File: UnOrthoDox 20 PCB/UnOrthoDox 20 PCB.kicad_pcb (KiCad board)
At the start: 2 copper layers, 76.2 x 94.2 mm, 81 parts, among them J1 Conn_01x02, SW1 SW_MX_HotSwap, SW10 SW_MX_HotSwap, SW11 SW_MX_HotSwap, SW12 SW_MX_HotSwap, SW13 SW_MX_HotSwap, SW14 SW_MX_HotSwap, SW15 SW_MX_HotSwap, SW16 SW_MX_HotSwap, SW16A1 SW_MX_HotSwap, SW17 SW_MX_HotSwap, SW17A1 SW_MX_HotSwap, SW18 SW_MX_HotSwap, SW19 SW_MX_HotSwap, SW2 SW_MX_HotSwap, SW20 SW_MX_HotSwap, SW3 SW_MX_HotSwap, SW4 SW_MX_HotSwap, SW5 SW_MX_HotSwap, SW6 SW_MX_HotSwap, SW7 SW_MX_HotSwap, SW8 SW_MX_HotSwap, SW8A1 SW_MX_HotSwap, SW9 SW_MX_HotSwap, U1 ProMicro

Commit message: Added 17
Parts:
- removed J1: Conn_01x02, Connector_PinHeader_2.54mm:PinHeader_1x02_P2.54mm_Vertical
- removed LED16A1, LED17A1, LED8A1: SK6812, Keyboard RGB:RGB_SK6812MINI-E
- removed RES1: TS-A002, Keyboard Common:YTS-A002
- removed ST1, ST2, ST3: Stabilizer_2u_MX, Keyboard Stabilizer:Stabilizer_Cherry_MX_2.00u
- removed SW16A1, SW17A1, SW8A1: SW_MX_HotSwap, Keyboard Switches:SW_MX_HotSwap
- removed SW_SLIDE_1: MSK12C02, Keyboard Common:MSK12C02
- added RZ1: RP2040-Zero, Keyboard Controllers:RP2040-Zero_reverse_mount_flipped, B.Cu at (147.8, 54.7)
- C1, C2, C3, C4: value 100nF -> C_Small; footprint Capacitor_SMD:C_0805_2012Metric_Pad1.18x1.45mm_HandSolder -> Capacitor_SMD:C_0603_1608Metric_Pad1.08x0.95mm_HandSolder
- ENC1, ENC2: footprint Keyboard Encoders:Encoder_Alps_EC11E_Offset_pad -> Keyboard Encoders:Encoder_Alps_EC11E_Small
- RGB1: renamed from LED1; value SK6812 -> SK6812MINI-E; footprint Keyboard RGB:RGB_SK6812MINI-E -> Keyboard RGB:MX_SK6812MINI-E_REVERSIBLE
- RGB10: renamed from LED10; value SK6812 -> SK6812MINI-E; footprint Keyboard RGB:RGB_SK6812MINI-E -> Keyboard RGB:MX_SK6812MINI-E_REVERSIBLE
- RGB11: renamed from LED11; value SK6812 -> SK6812MINI-E; footprint Keyboard RGB:RGB_SK6812MINI-E -> Keyboard RGB:MX_SK6812MINI-E_REVERSIBLE
- RGB12: renamed from LED12; value SK6812 -> SK6812MINI-E; footprint Keyboard RGB:RGB_SK6812MINI-E -> Keyboard RGB:MX_SK6812MINI-E_REVERSIBLE
- RGB13: renamed from LED13; value SK6812 -> SK6812MINI-E; footprint Keyboard RGB:RGB_SK6812MINI-E -> Keyboard RGB:MX_SK6812MINI-E_REVERSIBLE
- RGB14: renamed from LED14; value SK6812 -> SK6812MINI-E; footprint Keyboard RGB:RGB_SK6812MINI-E -> Keyboard RGB:MX_SK6812MINI-E_REVERSIBLE
- RGB15: renamed from LED15; value SK6812 -> SK6812MINI-E; footprint Keyboard RGB:RGB_SK6812MINI-E -> Keyboard RGB:MX_SK6812MINI-E_REVERSIBLE
- RGB16: renamed from LED16; value SK6812 -> SK6812MINI-E; footprint Keyboard RGB:RGB_SK6812MINI-E -> Keyboard RGB:MX_SK6812MINI-E_REVERSIBLE
- RGB17: renamed from LED17; value SK6812 -> SK6812MINI-E; footprint Keyboard RGB:RGB_SK6812MINI-E -> Keyboard RGB:MX_SK6812MINI-E_REVERSIBLE
- RGB18: renamed from LED18; value SK6812 -> SK6812MINI-E; footprint Keyboard RGB:RGB_SK6812MINI-E -> Keyboard RGB:MX_SK6812MINI-E_REVERSIBLE
- RGB19: renamed from LED19; value SK6812 -> SK6812MINI-E; footprint Keyboard RGB:RGB_SK6812MINI-E -> Keyboard RGB:MX_SK6812MINI-E_REVERSIBLE
- RGB2: renamed from LED2; value SK6812 -> SK6812MINI-E; footprint Keyboard RGB:RGB_SK6812MINI-E -> Keyboard RGB:MX_SK6812MINI-E_REVERSIBLE
- RGB20: renamed from LED20; value SK6812 -> SK6812MINI-E; footprint Keyboard RGB:RGB_SK6812MINI-E -> Keyboard RGB:MX_SK6812MINI-E_REVERSIBLE
- RGB3: renamed from LED3; value SK6812 -> SK6812MINI-E; footprint Keyboard RGB:RGB_SK6812MINI-E -> Keyboard RGB:MX_SK6812MINI-E_REVERSIBLE
- RGB4: renamed from LED4; value SK6812 -> SK6812MINI-E; footprint Keyboard RGB:RGB_SK6812MINI-E -> Keyboard RGB:MX_SK6812MINI-E_REVERSIBLE
- RGB5: renamed from LED5; value SK6812 -> SK6812MINI-E; footprint Keyboard RGB:RGB_SK6812MINI-E -> Keyboard RGB:MX_SK6812MINI-E_REVERSIBLE
- RGB6: renamed from LED6; value SK6812 -> SK6812MINI-E; footprint Keyboard RGB:RGB_SK6812MINI-E -> Keyboard RGB:MX_SK6812MINI-E_REVERSIBLE
- RGB7: renamed from LED7; value SK6812 -> SK6812MINI-E; footprint Keyboard RGB:RGB_SK6812MINI-E -> Keyboard RGB:MX_SK6812MINI-E_REVERSIBLE
- RGB8: renamed from LED8; value SK6812 -> SK6812MINI-E; footprint Keyboard RGB:RGB_SK6812MINI-E -> Keyboard RGB:MX_SK6812MINI-E_REVERSIBLE
- RGB9: renamed from LED9; value SK6812 -> SK6812MINI-E; footprint Keyboard RGB:RGB_SK6812MINI-E -> Keyboard RGB:MX_SK6812MINI-E_REVERSIBLE
- SW1, SW10, SW11, SW12, SW13, SW14, SW15, SW16, SW17, SW18, SW19, SW2, SW20, SW3, SW4, SW5, SW6, SW7, SW8, SW9: footprint Keyboard Switches:SW_MX_HotSwap -> Keyboard Switches:SW_MX_HotSwap_Reversible
- U1: value ProMicro -> SN74LV1T34DBV; footprint Keyboard Controllers:ArduinoProMicro-BackSide_special -> Package_TO_SOT_SMD:SOT-23-5; moved to B.Cu
- moved D18 16.0 mm to (130.6, 121.4)
- moved RGB16 15.2 mm to (176.9, 104.9), turned to 180 degrees
- moved RGB8 15.2 mm to (176.9, 66.8), turned to 180 degrees
- moved U1 13.6 mm to (126.3, 52.2), turned to 180 degrees
- moved RGB18 6.08 mm to (138.8, 123.9), turned to 180 degrees
- moved D20 5.28 mm to (168.7, 121.4)
- moved D12 5.10 mm to (168.8, 83.6)
- moved RGB1 5.08 mm to (119.8, 47.7), turned to 180 degrees
- moved RGB2 5.08 mm to (138.8, 47.7), turned to 180 degrees
- moved RGB3 5.08 mm to (157.9, 47.7), turned to 180 degrees
- moved RGB4 5.08 mm to (176.9, 47.7), turned to 180 degrees
- moved RGB5 5.08 mm to (119.8, 66.8), turned to 180 degrees
- moved RGB6 5.08 mm to (138.8, 66.8), turned to 180 degrees
- moved RGB7 5.08 mm to (157.9, 66.8), turned to 180 degrees
- moved RGB10 5.08 mm to (138.8, 85.8), turned to 180 degrees
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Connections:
- net C renamed Net-(D17-A)
- net ENC1 renamed EncA
- net ENC2 renamed EncB
- C1 pad 1: Enc1A -> Enc_1
- C2 pad 2: Enc1B -> Enc_2
- C3 pad 1: Enc2A -> Enc_1
- C4 pad 2: Enc2B -> Enc_3
- D16 pad 2: B -> Net-(D16-A)
- D18 pad 2: Net-(D18-Pad2) -> Net-(D18-A)
- D8 pad 2: A -> Net-(D8-A)
- ENC1 pad A: Enc1A -> Enc_1
- ENC1 pad B: Enc1B -> Enc_2
- ENC2 pad A: Enc2A -> Enc_1
- ENC2 pad B: Enc2B -> Enc_3
- RGB1 pad 1: GND -> +5V
- RGB1 pad 2: RGB -> Net-(RGB1-DOUT)
- RGB1 pad 3: VCC -> GND
- RGB1 pad 4: Net-(LED1-Pad4) -> RGB_5
- RGB10 pad 1: GND -> +5V
- RGB10 pad 2: Net-(LED10-Pad2) -> Net-(RGB10-DOUT)
- RGB10 pad 3: VCC -> GND
- RGB10 pad 4: Net-(LED10-Pad4) -> Net-(RGB10-DIN)
- RGB11 pad 1: GND -> +5V
- RGB11 pad 2: Net-(LED10-Pad4) -> Net-(RGB11-DOUT)
- RGB11 pad 3: VCC -> GND
- RGB11 pad 4: Net-(LED11-Pad4) -> Net-(RGB10-DOUT)
- RGB12 pad 1: GND -> +5V
- RGB12 pad 2: Net-(LED11-Pad4) -> Net-(RGB12-DOUT)
- RGB12 pad 3: VCC -> GND
- RGB12 pad 4: Net-(LED12-Pad4) -> Net-(RGB11-DOUT)
- RGB13 pad 1: GND -> +5V
- RGB13 pad 3: VCC -> GND
- RGB13 pad 4: Net-(LED13-Pad4) -> Net-(RGB12-DOUT)
- RGB14 pad 1: GND -> +5V
- RGB14 pad 3: VCC -> GND
- RGB15 pad 1: GND -> +5V
- RGB15 pad 3: VCC -> GND
- RGB16 pad 1: GND -> +5V
- RGB16 pad 2: Net-(LED12-Pad4) -> Net-(RGB16-DOUT)
- RGB16 pad 3: VCC -> GND
- RGB17 pad 1: GND -> +5V
- RGB17 pad 2: Net-(LED13-Pad4) -> Net-(RGB17-DOUT)
- RGB17 pad 3: VCC -> GND
- RGB17 pad 4: Net-(LED17-Pad4) -> Net-(RGB16-DOUT)
- RGB18 pad 1: GND -> +5V
- RGB18 pad 2: Net-(LED17-Pad4) -> Net-(RGB18-DOUT)
- RGB18 pad 3: VCC -> GND
- RGB18 pad 4: Net-(LED17A1-Pad4) -> Net-(RGB17-DOUT)
- RGB19 pad 1: GND -> +5V
- RGB19 pad 2: Net-(LED17A1-Pad4) -> Net-(RGB19-DOUT)
- RGB19 pad 3: VCC -> GND
- RGB19 pad 4: Net-(LED19-Pad4) -> Net-(RGB18-DOUT)
- RGB2 pad 1: GND -> +5V
- RGB2 pad 2: Net-(LED1-Pad4) -> Net-(RGB2-DOUT)
- RGB2 pad 3: VCC -> GND
- RGB2 pad 4: Net-(LED2-Pad4) -> Net-(RGB1-DOUT)
- RGB20 pad 1: GND -> +5V
- RGB20 pad 2: Net-(LED19-Pad4) -> unconnected-(RGB20-DOUT-Pad2)
- RGB20 pad 3: VCC -> GND
- RGB20 pad 4: unconnected-(LED20-Pad4) -> Net-(RGB19-DOUT)
- RGB3 pad 1: GND -> +5V
- RGB3 pad 2: Net-(LED2-Pad4) -> Net-(RGB3-DOUT)
- RGB3 pad 3: VCC -> GND
- RGB3 pad 4: Net-(LED3-Pad4) -> Net-(RGB2-DOUT)
- RGB4 pad 1: GND -> +5V
- RGB4 pad 2: Net-(LED3-Pad4) -> Net-(RGB4-DOUT)
- RGB4 pad 3: VCC -> GND
- RGB4 pad 4: Net-(LED4-Pad4) -> Net-(RGB3-DOUT)
- RGB5 pad 1: GND -> +5V
- RGB5 pad 3: VCC -> GND
- RGB5 pad 4: Net-(LED5-Pad4) -> Net-(RGB4-DOUT)
- RGB6 pad 1: GND -> +5V
- RGB6 pad 3: VCC -> GND
- RGB7 pad 1: GND -> +5V
- RGB7 pad 3: VCC -> GND
- RGB8 pad 1: GND -> +5V
- RGB8 pad 2: Net-(LED4-Pad4) -> Net-(RGB8-DOUT)
- RGB8 pad 3: VCC -> GND
- RGB9 pad 1: GND -> +5V
- RGB9 pad 2: Net-(LED5-Pad4) -> Net-(RGB10-DIN)
- RGB9 pad 3: VCC -> GND
- RGB9 pad 4: Net-(LED10-Pad2) -> Net-(RGB8-DOUT)
- SW16 pad 1: Col3 -> Net-(D16-A)
- SW16 pad 2: B -> Col3
- SW18 pad 1: Col1 -> Net-(D18-A)
- SW18 pad 2: Net-(D18-Pad2) -> Col1
- SW8 pad 1: Col3 -> Net-(D8-A)
- SW8 pad 2: A -> Col3
- U1 pad 4: GND -> RGB_5
- U1 pad 5: Enc1B -> +5V
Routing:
- net +5V: track 0.00 -> 485.6 mm, vias 0 -> 25
- net VCC: track 410.0 -> 0.00 mm, vias 25 -> 0
- net Net-(RGB4-DOUT): track 0.00 -> 90.2 mm, vias 0 -> 4
- net Net-(RGB16-DOUT): track 0.00 -> 83.2 mm, vias 0 -> 3
- net Net-(RGB12-DOUT): track 0.00 -> 82.8 mm, vias 0 -> 3
- net Net-(RGB8-DOUT): track 0.00 -> 82.2 mm, vias 0 -> 3
- net Enc_1: track 0.00 -> 66.9 mm
- net /RAW: track 46.4 -> 0.00 mm, vias 1 -> 0
- net Net-(RGB15-DOUT): track 60.2 -> 17.9 mm, vias 4 -> 2
- net Net-(LED4-Pad4): track 41.9 -> 0.00 mm, vias 2 -> 0
- net Net-(RGB7-DOUT): track 58.4 -> 17.7 mm, vias 4 -> 2
- net Net-(LED13-Pad4): track 40.2 -> 0.00 mm, vias 2 -> 0
- net Net-(RES1-Pad1): track 40.0 -> 0.00 mm, vias 1 -> 0
- net Net-(LED12-Pad4): track 38.9 -> 0.00 mm, vias 2 -> 0
- net Net-(LED17A1-Pad4): track 38.6 -> 0.00 mm, vias 3 -> 0
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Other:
- board size 76.2 x 94.2 mm -> 76.2 x 96.7 mm
- board text removed: "- +"
- board text removed: "RESET"

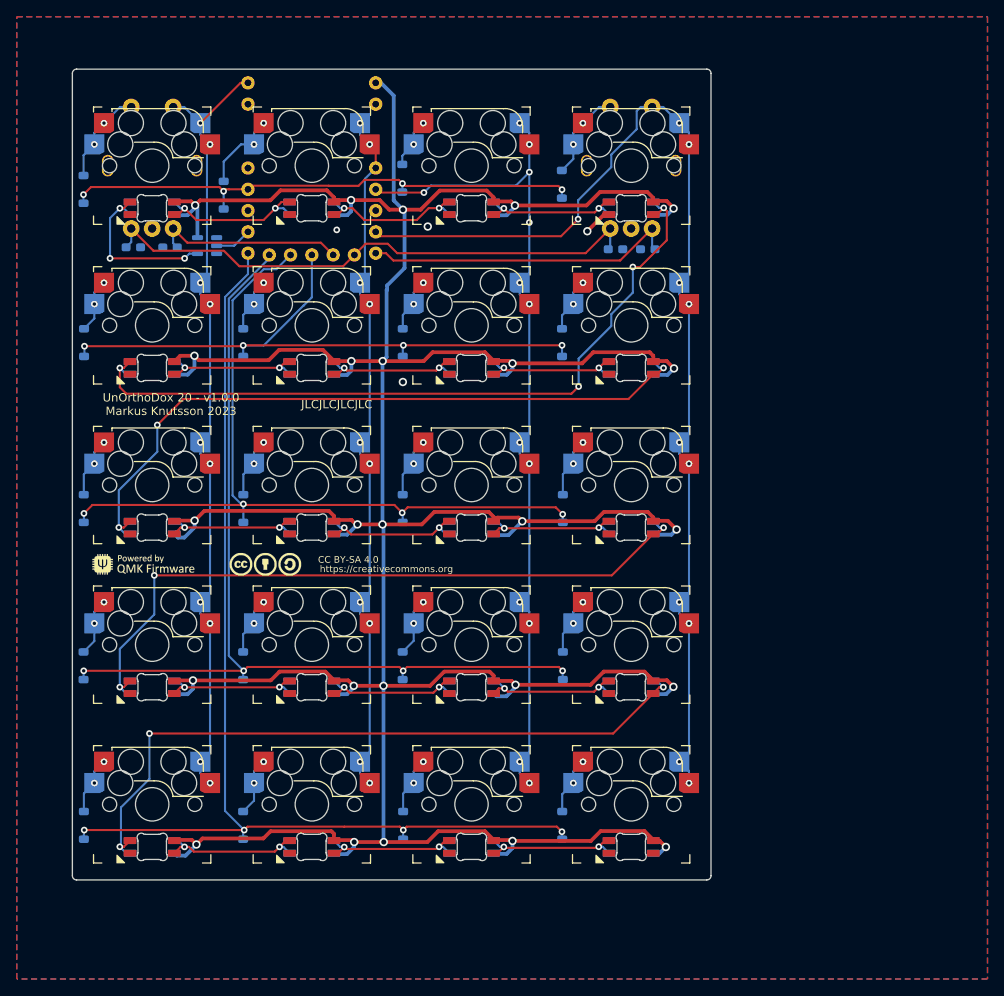
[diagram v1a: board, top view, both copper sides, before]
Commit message: Final tweaks 17/20 PCB
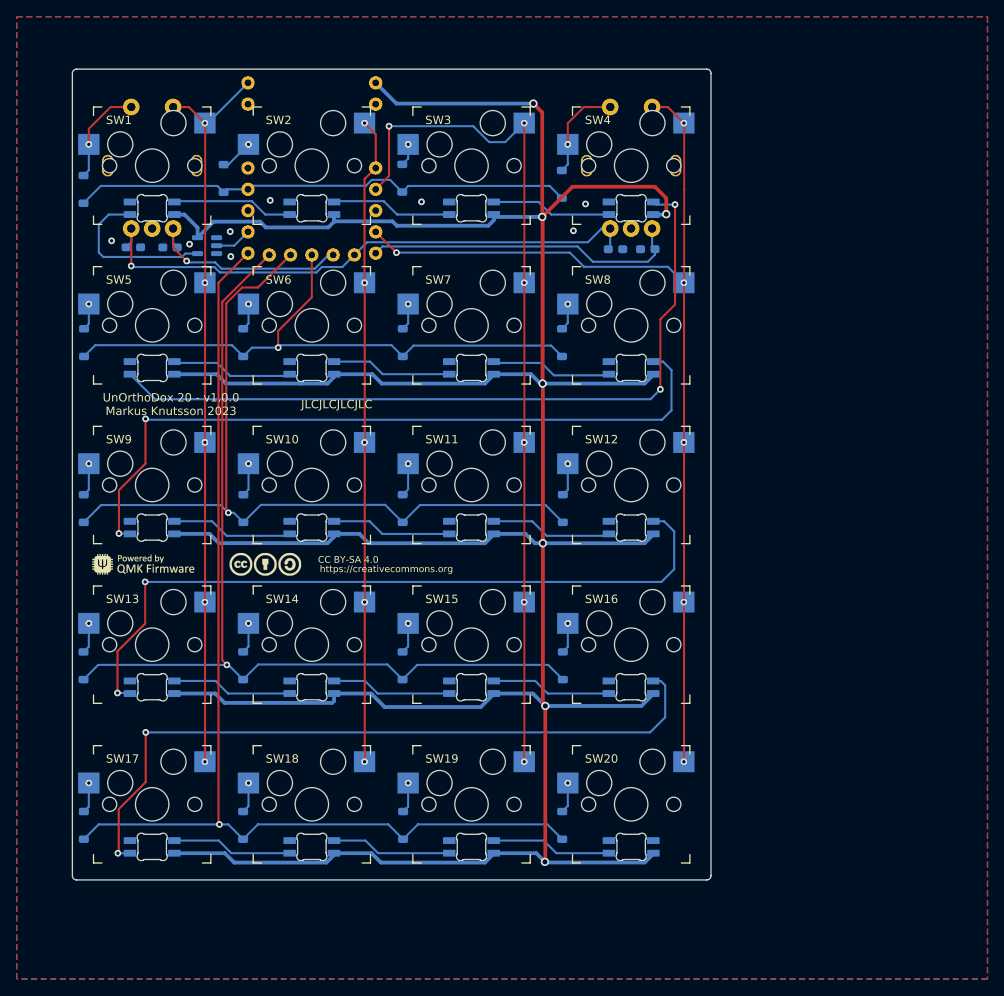
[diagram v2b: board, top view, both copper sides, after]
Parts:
- RGB1, RGB10, RGB11, RGB12, RGB13, RGB14, RGB15, RGB16, RGB17, RGB18, RGB19, RGB2, RGB20, RGB3, RGB4, RGB5, RGB6, RGB7, RGB8, RGB9: footprint Keyboard RGB:MX_SK6812MINI-E_REVERSIBLE -> Keyboard RGB:RGB_SK6812MINI-E
- RZ1: footprint Keyboard Controllers:RP2040-Zero_reverse_mount_flipped -> Keyboard Controllers:RP2040-Zero_reverse_mount_flipped_less_pins
- SW1, SW10, SW11, SW12, SW13, SW14, SW15, SW16, SW17, SW18, SW19, SW2, SW20, SW3, SW4, SW5, SW6, SW7, SW8, SW9: footprint Keyboard Switches:SW_MX_HotSwap_Reversible -> Keyboard Switches:SW_MX_HotSwap
- moved RGB17 5.08 mm to (119.8, 129.0)
- moved RGB18 5.08 mm to (138.8, 129.0)
- moved RGB19 5.08 mm to (157.9, 129.0)
- moved RGB20 5.08 mm to (176.9, 129.0)
- moved RGB1 5.08 mm to (119.8, 52.8)
- moved RGB10 5.08 mm to (138.8, 90.9)
- moved RGB11 5.08 mm to (157.9, 90.9)
- moved RGB12 5.08 mm to (176.9, 90.9)
- moved RGB13 5.08 mm to (119.8, 110.0)
- moved RGB14 5.08 mm to (138.8, 110.0)
- moved RGB15 5.08 mm to (157.9, 110.0)
- moved RGB16 5.08 mm to (176.9, 110.0)
- moved RGB2 5.08 mm to (138.8, 52.8)
- moved RGB3 5.08 mm to (157.9, 52.8)
- moved RGB4 5.08 mm to (176.9, 52.8)
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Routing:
- net +5V: track 485.6 -> 423.0 mm, vias 25 -> 7
- net Col3: track 130.1 -> 120.1 mm, vias 11 -> 6
- net Col0: track 94.7 -> 88.0 mm, vias 10 -> 5
- net Col1: track 83.6 -> 77.3 mm, vias 10 -> 5
- net Net-(D2-A): track 9.84 -> 3.96 mm, vias 2 -> 1
- net Row1: track 77.9 -> 73.1 mm, vias 4 -> 1
- net Net-(RGB8-DOUT): track 82.2 -> 87.0 mm, vias 3 -> 2
- net Net-(RGB1-DOUT): track 19.1 -> 14.5 mm, vias 2 -> 0
- net Net-(RGB12-DOUT): track 82.8 -> 87.4 mm, vias 3 -> 2
- net Net-(RGB2-DOUT): track 18.6 -> 14.5 mm, vias 2 -> 0
- net Net-(RGB10-DOUT): track 18.1 -> 14.4 mm, vias 2 -> 0
- net Net-(RGB14-DOUT): track 18.0 -> 14.4 mm, vias 2 -> 0
- net Row0: track 63.9 -> 60.4 mm, vias 4 -> 0
- net Net-(RGB15-DOUT): track 17.9 -> 14.4 mm, vias 2 -> 0
- net Net-(RGB17-DOUT): track 17.9 -> 14.4 mm, vias 2 -> 0
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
